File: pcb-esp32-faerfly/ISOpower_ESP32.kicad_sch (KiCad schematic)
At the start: 24 parts, among them J10 ESPpin1-4, J2 SDI/SDO, J4 gpio-B, J5 touch0, J6 Touch Pins, J7 DAC/ADC, J9 i2c-header, U2 AMS1117-3.3, U3 ESP32-WROOM-32

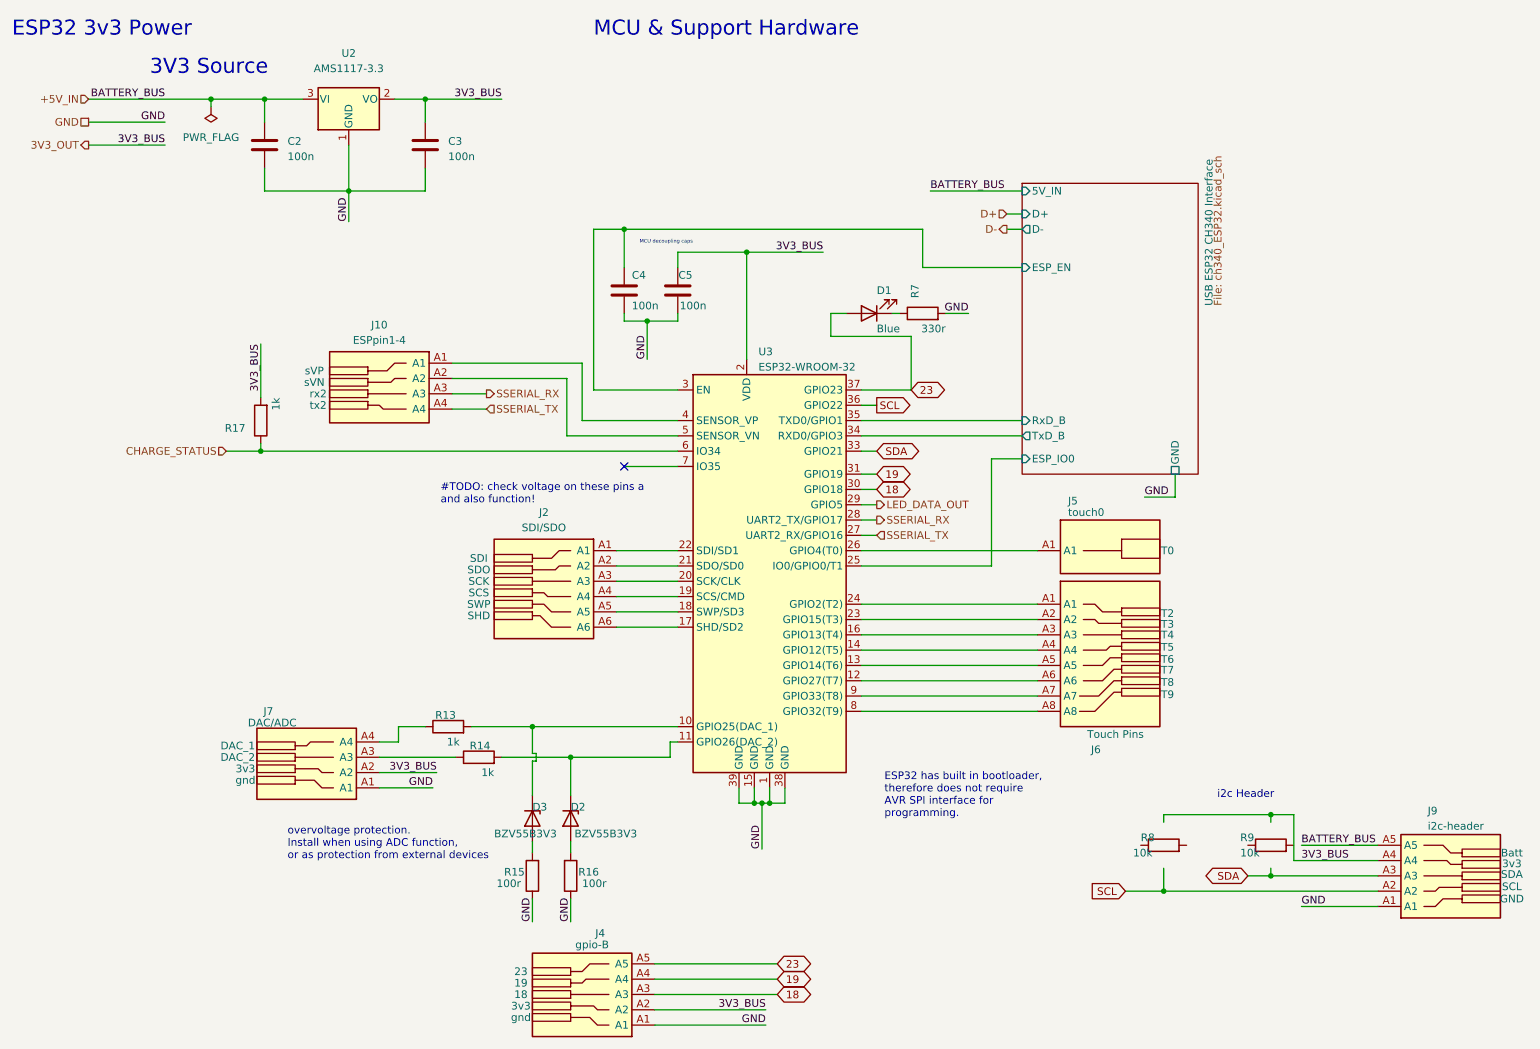
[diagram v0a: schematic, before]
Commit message: added JLC part numbers
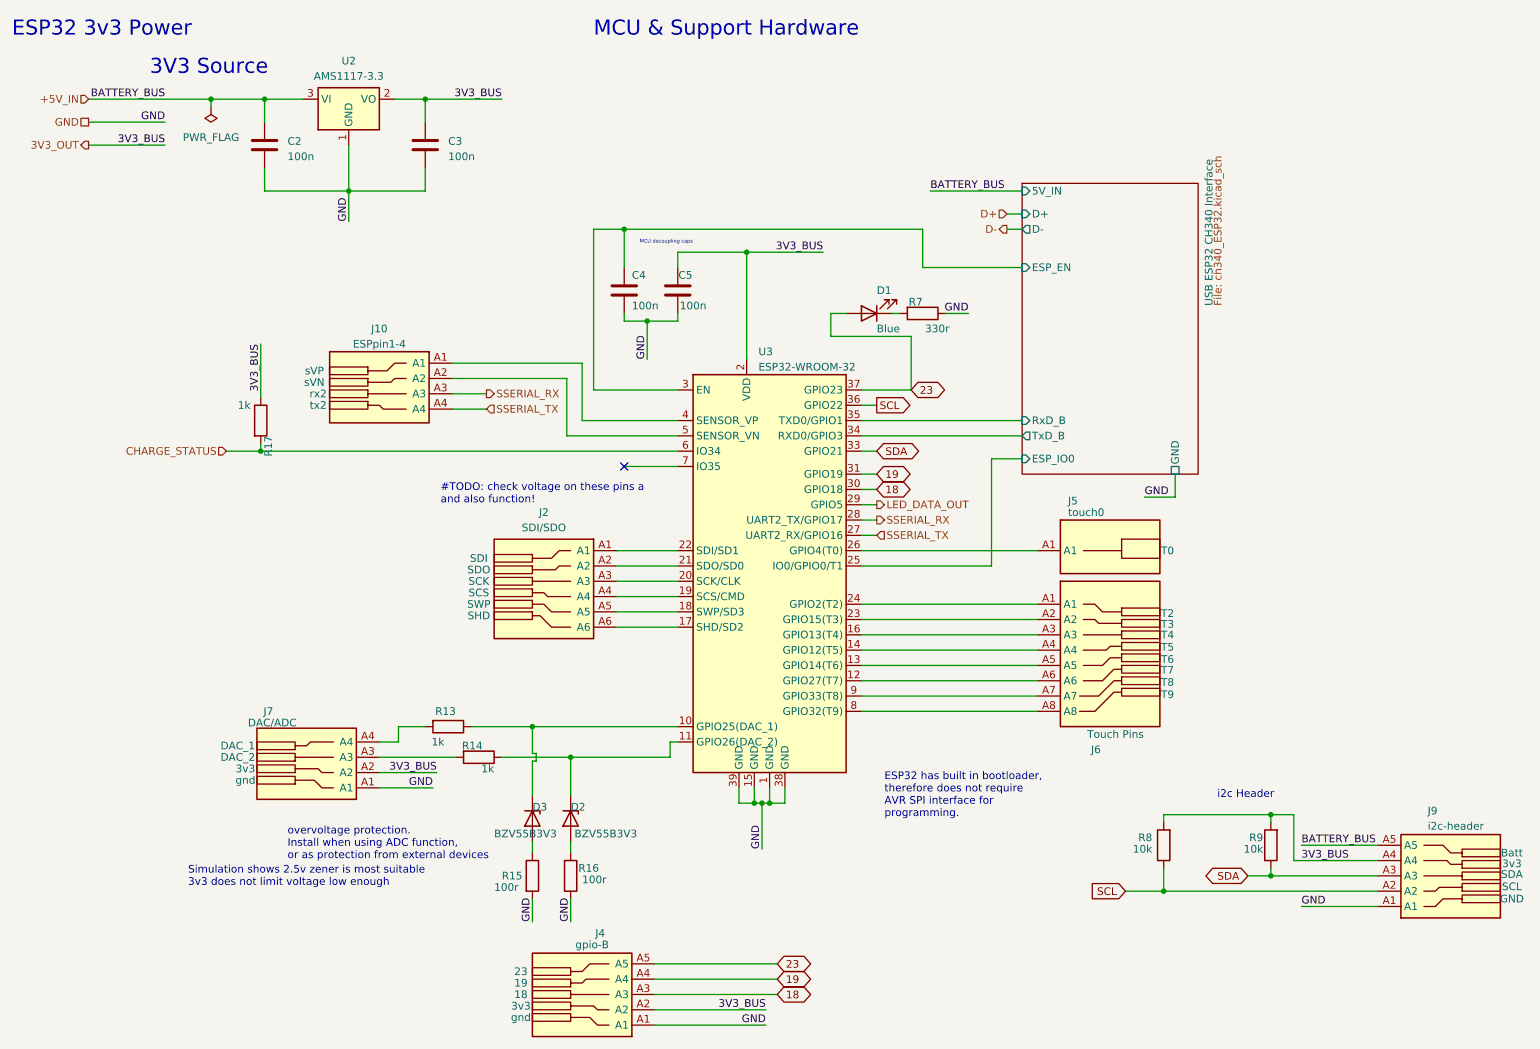
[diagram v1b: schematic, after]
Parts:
- D1: footprint LED_SMD:LED_0805_2012Metric_Pad1.15x1.40mm_HandSolder -> Diode_SMD:D_0805_2012Metric_Pad1.15x1.40mm_HandSolder; symbol 000_Diodes_Immo:LED_0805_smd -> 000_Diodes_Immo:LED_0805_Yellow; Cost (none) -> 0.0158; JLCpart (none) -> C84261
- D2, D3: symbol Diode:BZV55B3V3 -> 000_Diodes_Immo:zener_diode_2v7; Cost (none) -> 0.0221; JLCpart (none) -> C268735
- R13, R14, R17: symbol 000_Resistors_Immo:Resistor_0805 -> 000_Resistors_Immo:1k; Cost (none) -> 0.0082; JLCpart (none) -> C218388
- R15, R16: symbol 000_Resistors_Immo:Resistor_0805 -> 000_Resistors_Immo:100r; Cost (none) -> 0.0093; JLCpart (none) -> C217766
- R7: symbol 000_Resistors_Immo:Resistor_0805 -> 000_Resistors_Immo:330r; Cost (none) -> 0.0016; JLCpart (none) -> C3017834
- U2: symbol Regulator_Linear:AMS1117-3.3 -> 000_IC_immo:AMS1117-3.3; Cost (none) -> 0.0488; JLCpart (none) -> C2992570
- U3: Cost (none) -> 3.5016; JLCpart (none) -> C473012 - C529577
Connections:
- net 3V3_OUT: now also R17.1, R8.2, R9.2; no longer R17.2
- net CHARGE_STATUS: now also R17.2; no longer R17.1
- net GND: now also R15.2, R7.1; no longer R15.1, R7.2
- net SCL: now also R8.1
- net SDA: now also R9.1
- net at D2.1 (K), U3.11 (GPIO26(DAC_2)): now also R14.1; no longer R14.2
- net at D3.1 (K), U3.10 (GPIO25(DAC_1)): now also R13.1; no longer R13.2
- net at J7.A3: now also R14.2; no longer R14.1
- net at J7.A4: now also R13.2; no longer R13.1
- net at D3.2 (A): now also R15.1; no longer R15.2
- net at D1.1 (K): now also R7.2; no longer R7.1
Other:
- note added: "Simulation shows 2.5v zener is most suitable 3v3 does not limit voltage low enough"
- moved on the sheet: R13, R14, R15, R16, R17, R7, R8, R9

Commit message: Added Complete BOM
Ready for Parts Shopping!
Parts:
- J10, J2, J4, J5, J6, J7, J9: now left out of the parts list
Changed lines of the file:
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@@
   )
   (symbol (lib_id "000-edge-connectors-immo:1-pin-edge-touch-XL") (at 200.66 115.57 0) (unit 1)
-    (in_bom yes) (on_board yes) (dnp no)
+    (in_bom no) (on_board yes) (dnp no)
     (property "Reference" "J5" (at 190.5 94.615 0)
       (effects (font (size 1.27 1.27)) (justify left))
@@
   )
   (symbol (lib_id "000-edge-connectors-immo:5-pin-edge-touch") (at 257.175 146.685 0) (mirror x) (unit 1)
-    (in_bom yes) (on_board yes) (dnp no)
+    (in_bom no) (on_board yes) (dnp no)
     (property "Reference" "J9" (at 250.19 146.05 0)
       (effects (font (size 1.27 1.27)) (justify left))
@@
   )
   (symbol (lib_id "000-edge-connectors-immo:4-pin-edge-touch") (at 60.96 138.43 180) (unit 1)
-    (in_bom yes) (on_board yes) (dnp no)
+    (in_bom no) (on_board yes) (dnp no)
     (property "Reference" "J7" (at 57.785 129.54 0)
       (effects (font (size 1.27 1.27)))
@@
   )
   (symbol (lib_id "000-edge-connectors-immo:4-pin-edge-touch") (at 73.025 75.565 0) (mirror y) (unit 1)
-    (in_bom yes) (on_board yes) (dnp no)
+    (in_bom no) (on_board yes) (dnp no)
     (property "Reference" "J10" (at 76.2 66.04 0)
       (effects (font (size 1.27 1.27)))
@@
   )
   (symbol (lib_id "000-edge-connectors-immo:8-pin-edge-touch") (at 200.66 127 0) (unit 1)
-    (in_bom yes) (on_board yes) (dnp no)
+    (in_bom no) (on_board yes) (dnp no)
     (property "Reference" "J6" (at 194.31 135.89 0)
       (effects (font (size 1.27 1.27)) (justify left))
@@
   )
   (symbol (lib_id "000-edge-connectors-immo:6-pin-edge-touch") (at 100.33 118.11 0) (mirror y) (unit 1)
-    (in_bom yes) (on_board yes) (dnp no)
+    (in_bom no) (on_board yes) (dnp no)
     (property "Reference" "J2" (at 103.505 96.52 0)
       (effects (font (size 1.27 1.27)))
@@
   )
   (symbol (lib_id "000-edge-connectors-immo:5-pin-edge-touch") (at 106.68 166.37 180) (unit 1)
-    (in_bom yes) (on_board yes) (dnp no)
+    (in_bom no) (on_board yes) (dnp no)
     (property "Reference" "J4" (at 113.665 166.37 0)
       (effects (font (size 1.27 1.27)) (justify left))
